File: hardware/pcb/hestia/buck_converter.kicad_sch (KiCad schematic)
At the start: 20 parts, among them U1 LM2655MTC-3.3/NOPB

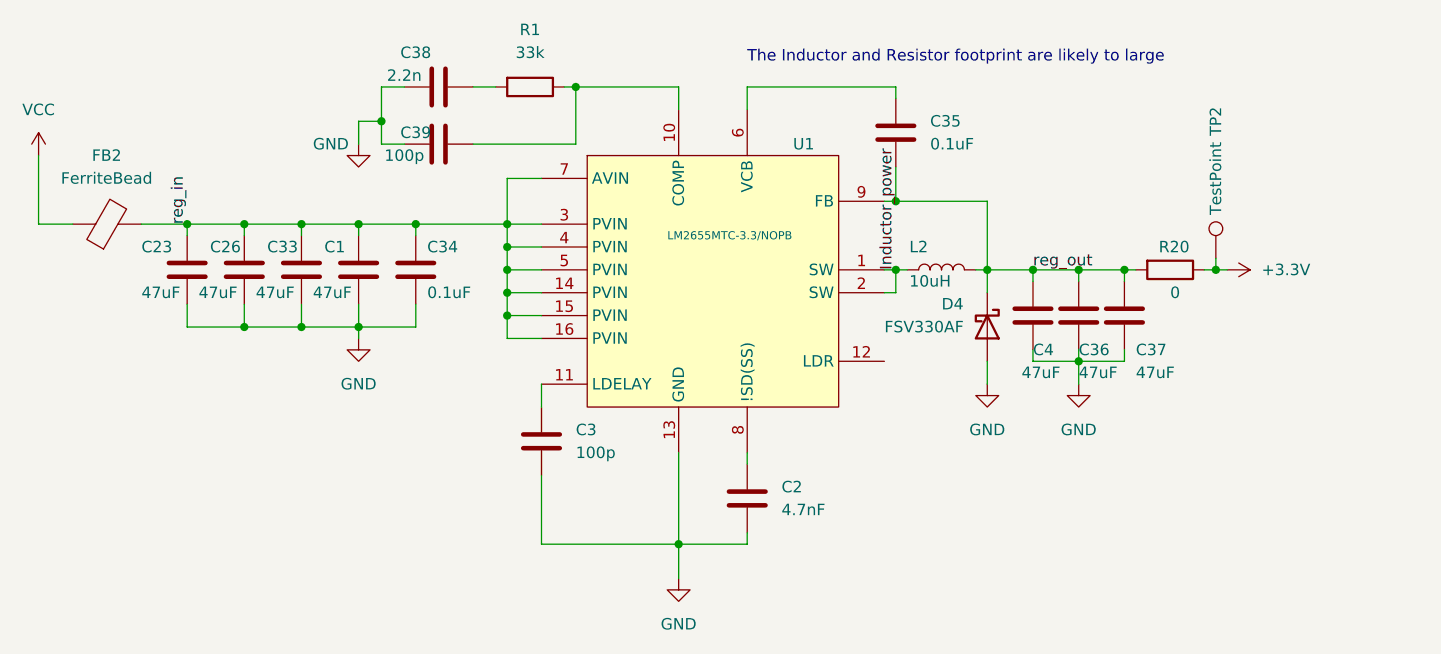
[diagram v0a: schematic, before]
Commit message: edit some component values
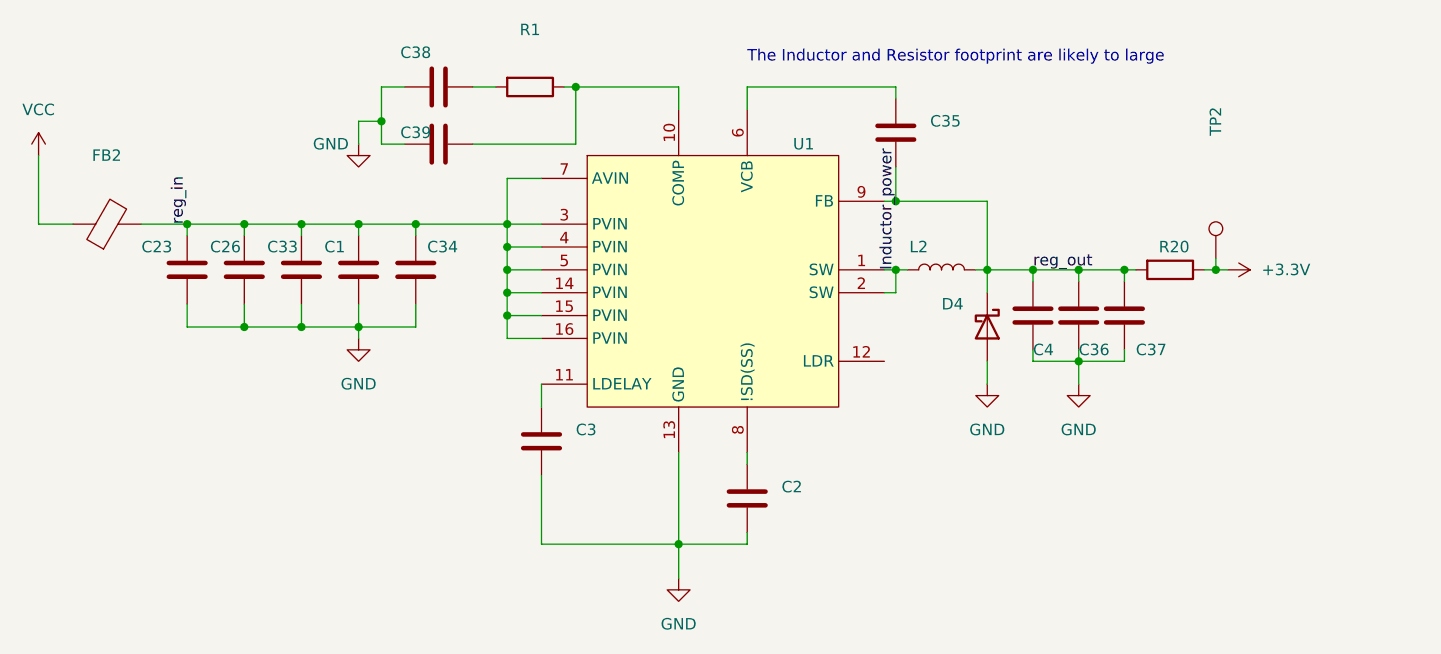
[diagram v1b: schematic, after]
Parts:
- C1, C23, C26, C33, C36, C37, C4: value 47uF -> (none); footprint Capacitor_SMD:C_0805_2012Metric_Pad1.18x1.45mm_HandSolder -> (none)
- C2: value 4.7nF -> (none); footprint Capacitor_SMD:C_0603_1608Metric_Pad1.08x0.95mm_HandSolder -> (none)
- C3, C39: value 100p -> (none); footprint Capacitor_SMD:C_0603_1608Metric_Pad1.08x0.95mm_HandSolder -> (none)
- C34, C35: value 0.1uF -> (none); footprint Capacitor_SMD:C_0603_1608Metric_Pad1.08x0.95mm_HandSolder -> (none)
- C38: value 2.2n -> (none); footprint Capacitor_SMD:C_0603_1608Metric_Pad1.08x0.95mm_HandSolder -> (none)
- D4: value FSV330AF -> (none); footprint Hestia:DO-214AD (SMAF) -> (none)
- FB2: value FerriteBead -> (none); footprint Resistor_SMD:R_0805_2012Metric_Pad1.20x1.40mm_HandSolder -> (none)
- L2: value 10uH -> (none); footprint Inductor_SMD:L_Coilcraft_LPS5030 -> (none)
- R1: value 33k -> (none); footprint Resistor_SMD:R_0603_1608Metric_Pad0.98x0.95mm_HandSolder -> (none)
- R20: value 0 -> (none); footprint Resistor_SMD:R_1210_3225Metric_Pad1.30x2.65mm_HandSolder -> (none)
- TP2: value TestPoint -> (none); footprint TestPoint:TestPoint_Pad_2.0x2.0mm -> (none)
- U1: value LM2655MTC-3.3/NOPB -> (none); footprint Package_SO:TSSOP-16_4.4x5mm_P0.65mm -> (none)

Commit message: Terminate pin 12 (LDR) on LM2655 to fix ERC warning
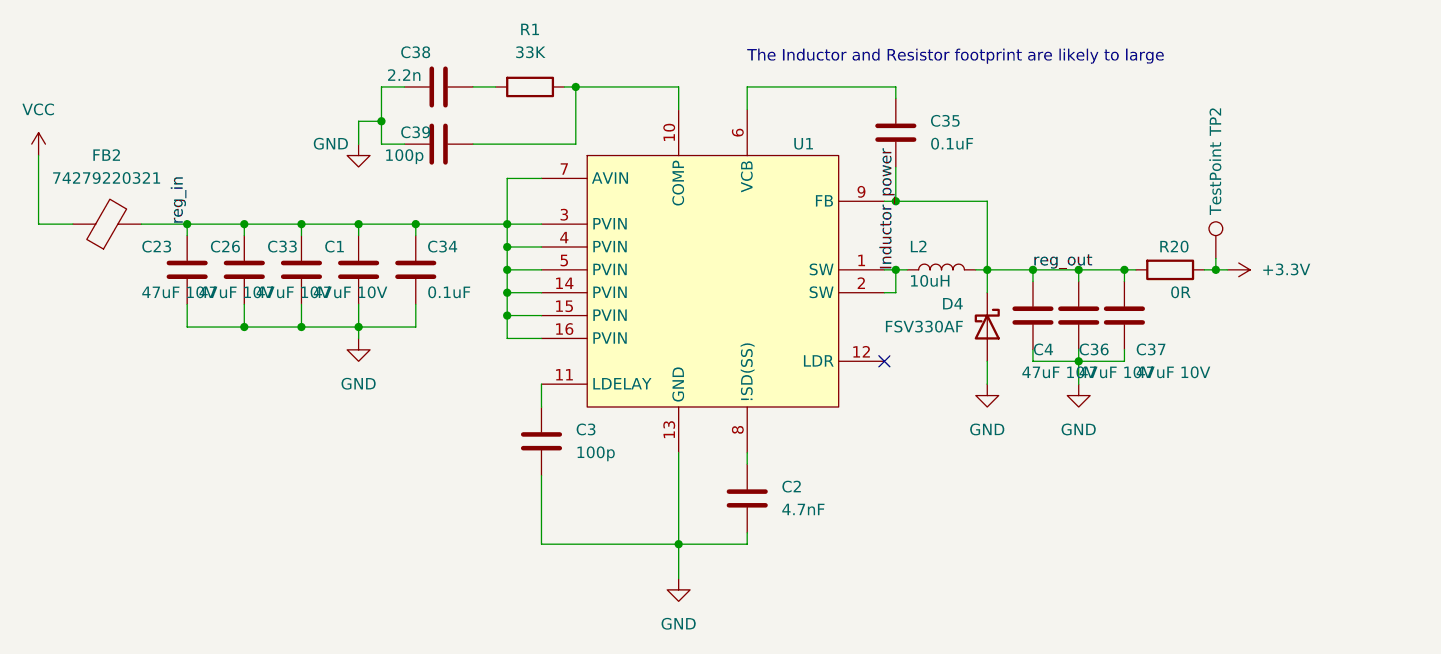
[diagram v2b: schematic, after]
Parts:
- C1, C23, C26, C33, C36, C37, C4: value (none) -> 47uF 10V; footprint (none) -> Capacitor_SMD:C_0805_2012Metric_Pad1.18x1.45mm_HandSolder
- C2: value (none) -> 4.7nF; footprint (none) -> Capacitor_SMD:C_0603_1608Metric_Pad1.08x0.95mm_HandSolder
- C3, C39: value (none) -> 100p; footprint (none) -> Capacitor_SMD:C_0603_1608Metric_Pad1.08x0.95mm_HandSolder
- C34, C35: value (none) -> 0.1uF; footprint (none) -> Capacitor_SMD:C_0603_1608Metric_Pad1.08x0.95mm_HandSolder
- C38: value (none) -> 2.2n; footprint (none) -> Capacitor_SMD:C_0603_1608Metric_Pad1.08x0.95mm_HandSolder
- D4: value (none) -> FSV330AF; footprint (none) -> Hestia:DO-214AD (SMAF)
- FB2: value (none) -> 74279220321; footprint (none) -> Resistor_SMD:R_0805_2012Metric_Pad1.20x1.40mm_HandSolder
- L2: value (none) -> 10uH; footprint (none) -> Inductor_SMD:L_Coilcraft_LPS5030
- R1: value (none) -> 33K; footprint (none) -> Resistor_SMD:R_0603_1608Metric_Pad0.98x0.95mm_HandSolder
- R20: value (none) -> 0R; footprint (none) -> Resistor_SMD:R_1210_3225Metric_Pad1.30x2.65mm_HandSolder
- TP2: value (none) -> TestPoint; footprint (none) -> TestPoint:TestPoint_Pad_2.0x2.0mm
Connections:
- no-connect marks 0 -> 1

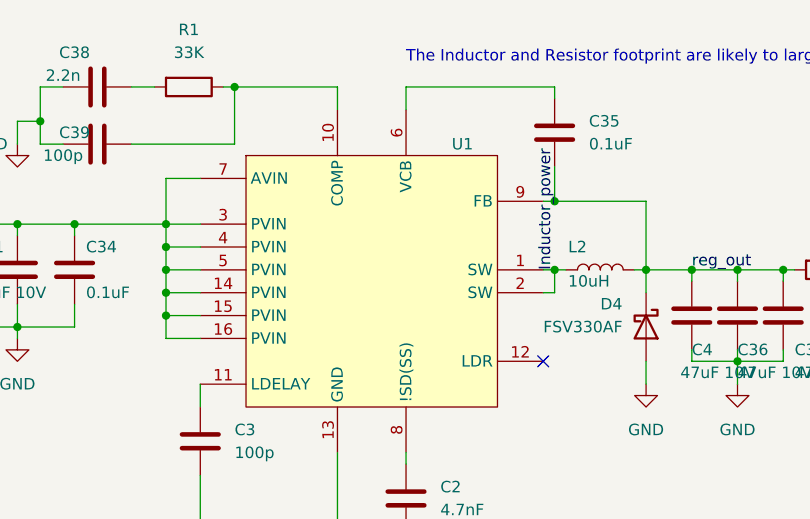
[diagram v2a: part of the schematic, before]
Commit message: Bump version to 2.0, add title to all schematic pages
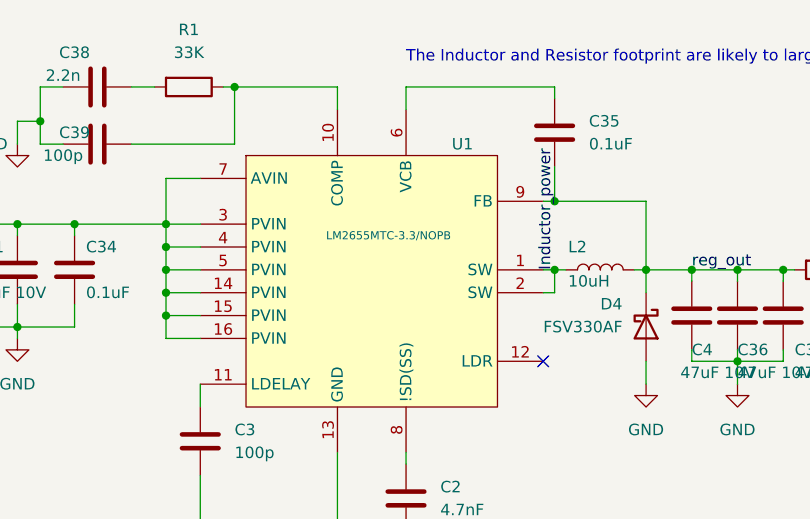
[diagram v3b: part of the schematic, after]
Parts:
- U1: value (none) -> LM2655MTC-3.3/NOPB; footprint (none) -> Package_SO:TSSOP-16_4.4x5mm_P0.65mm
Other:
- company: (none) -> Mawson Rovers
- title: (none) -> Hestia
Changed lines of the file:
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@@
 (kicad_sch (version 20211123) (generator eeschema)
   (paper "A4")
+  (title_block
+    (title "Hestia")
+    (date "2022-07-14")
+    (rev "2.0")
+    (company "Mawson Rovers")
+  )
   (junction (at 93.345 85.725) (diameter 0) (color 0 0 0 0)
   )
@@
       (effects (font (size 1.27 1.27)) (justify left))
     )
-    (property "Value" "" (id 1) (at 146.685 86.995 0)
+    (property "Value" "LM2655MTC-3.3/NOPB" (id 1) (at 146.685 86.995 0)
       (effects (font (size 0.9 0.9)) (justify left))
     )
-    (property "Footprint" "" (id 2) (at 155.575 95.885 0)
-      (effects (font (size 1.27 1.27)) hide)
-    )
+    (property "Footprint" "Package_SO:TSSOP-16_4.4x5mm_P0.65mm" (id 2) (at 155.575 95.885 0)
+      (effects (font (size 1.27 1.27)) hide)
+    )

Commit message: corrected diode placement
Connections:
- net Inductor_power: now also D4.1 (K)
- net reg_out: no longer D4.1 (K)
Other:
- moved on the sheet: D4
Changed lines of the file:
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@@
   (junction (at 192.405 90.805) (diameter 0) (color 0 0 0 0)
+  )
+  (junction (at 172.085 93.345) (diameter 0) (color 0 0 0 0)
   )
   (junction (at 114.935 74.295) (diameter 0) (color 0 0 0 0)
@@
     (stroke (width 0) (type default) (color 0 0 0 0))
   )
-  (wire (pts (xy 182.245 90.805) (xy 182.245 93.345))
-    (stroke (width 0) (type default) (color 0 0 0 0))
-  )
   (wire (pts (xy 99.695 97.155) (xy 106.045 97.155))
     (stroke (width 0) (type default) (color 0 0 0 0))
@@
     (stroke (width 0) (type default) (color 0 0 0 0))
   )
-  (wire (pts (xy 182.245 100.965) (xy 182.245 103.505))
+  (wire (pts (xy 172.085 100.965) (xy 172.085 103.505))
     (stroke (width 0) (type default) (color 0 0 0 0))
   )
@@
     (pin "2")
   )
-  (symbol (lib_id "Device:D_Schottky") (at 182.245 97.155 270) (unit 1)
-    (in_bom yes) (on_board yes)
-    (property "Reference" "D4" (id 0) (at 177.165 94.615 90)
-      (effects (font (size 1.27 1.27)) (justify left))
-    )
-    (property "Value" "FSV330AF" (id 1) (at 170.815 97.155 90)
-      (effects (font (size 1.27 1.27)) (justify left))
-    )
-    (property "Footprint" "Hestia:DO-214AD (SMAF)" (id 2) (at 182.245 97.155 0)
-      (effects (font (size 1.27 1.27)) hide)
-    )
-    (property "Datasheet" "~" (id 3) (at 182.245 97.155 0)
+  (symbol (lib_id "Device:D_Schottky") (at 172.085 97.155 270) (unit 1)
+    (in_bom yes) (on_board yes)
+    (property "Reference" "D4" (id 0) (at 167.005 94.615 90)
+      (effects (font (size 1.27 1.27)) (justify left))
+    )
+    (property "Value" "FSV330AF" (id 1) (at 160.655 97.155 90)
+      (effects (font (size 1.27 1.27)) (justify left))
+    )
+    (property "Footprint" "Hestia:DO-214AD (SMAF)" (id 2) (at 172.085 97.155 0)
+      (effects (font (size 1.27 1.27)) hide)
+    )
+    (property "Datasheet" "~" (id 3) (at 172.085 97.155 0)
       (effects (font (size 1.27 1.27)) hide)
     )
@@
     (pin "2")
   )
-  (symbol (lib_id "power:GND") (at 182.245 103.505 0) (unit 1)
+  (symbol (lib_id "power:GND") (at 172.085 103.505 0) (unit 1)
     (in_bom yes) (on_board yes) (fields_autoplaced)
-    (property "Reference" "#PWR04" (id 0) (at 182.245 109.855 0)
-      (effects (font (size 1.27 1.27)) hide)
-    )
-    (property "Value" "GND" (id 1) (at 182.245 108.585 0))
-    (property "Footprint" "" (id 2) (at 182.245 103.505 0)
-      (effects (font (size 1.27 1.27)) hide)
-    )
-    (property "Datasheet" "" (id 3) (at 182.245 103.505 0)
-      (effects (font (size 1.27 1.27)) hide)
-    )
+    (property "Reference" "#PWR04" (id 0) (at 172.085 109.855 0)
+      (effects (font (size 1.27 1.27)) hide)
+    )
+    (property "Value" "GND" (id 1) (at 172.085 108.585 0))
+    (property "Footprint" "" (id 2) (at 172.085 103.505 0)
+      (effects (font (size 1.27 1.27)) hide)
+    )
+    (property "Datasheet" "" (id 3) (at 172.085 103.505 0)
+      (effects (font (size 1.27 1.27)) hide)
+    )

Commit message: correct C35 capcitor placement
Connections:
- net Inductor_power: now also C35.2
- net reg_out: no longer C35.2
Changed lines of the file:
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@@
   (junction (at 106.045 85.725) (diameter 0) (color 0 0 0 0)
-  )
-  (junction (at 172.085 83.185) (diameter 0) (color 0 0 0 0)
   )
   (junction (at 128.905 93.345) (diameter 0) (color 0 0 0 0)
@@
     (stroke (width 0) (type default) (color 0 0 0 0))
   )
+  (wire (pts (xy 172.085 79.375) (xy 172.085 90.805))
+    (stroke (width 0) (type default) (color 0 0 0 0))
+  )
   (wire (pts (xy 76.835 85.725) (xy 80.645 85.725))
     (stroke (width 0) (type default) (color 0 0 0 0))
@@
     (stroke (width 0) (type default) (color 0 0 0 0))
   )
-  (wire (pts (xy 172.085 83.185) (xy 182.245 83.185))
+  (wire (pts (xy 170.815 83.185) (xy 182.245 83.185))
     (stroke (width 0) (type default) (color 0 0 0 0))
   )
@@
     (stroke (width 0) (type default) (color 0 0 0 0))
   )
-  (wire (pts (xy 170.815 83.185) (xy 172.085 83.185))
-    (stroke (width 0) (type default) (color 0 0 0 0))
-  )
   (wire (pts (xy 114.935 76.835) (xy 114.935 74.295))
     (stroke (width 0) (type default) (color 0 0 0 0))
   )
-  (wire (pts (xy 172.085 79.375) (xy 172.085 83.185))
-    (stroke (width 0) (type default) (color 0 0 0 0))
-  )

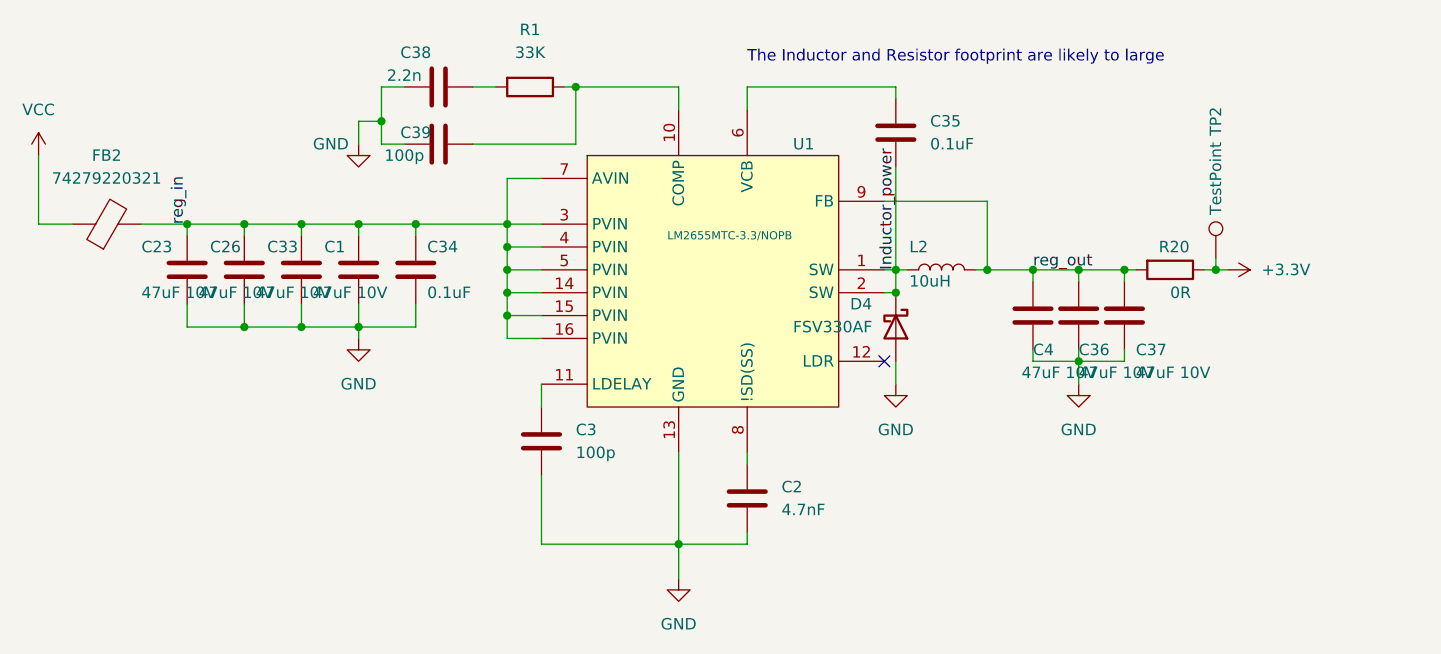
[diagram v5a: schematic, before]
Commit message: don't update pcb from schematic yet. added and changed footprint info on schematic for 1.5mm pitch term pads, crystals, jtag vcc jumper. a bunch of components are out of sync with the pcb, the schematic is unaware that the components are already on the PCB. some components from the first versions were not in the hestia parts library - hopefully this commit adds them back? was a commit made without a pull?
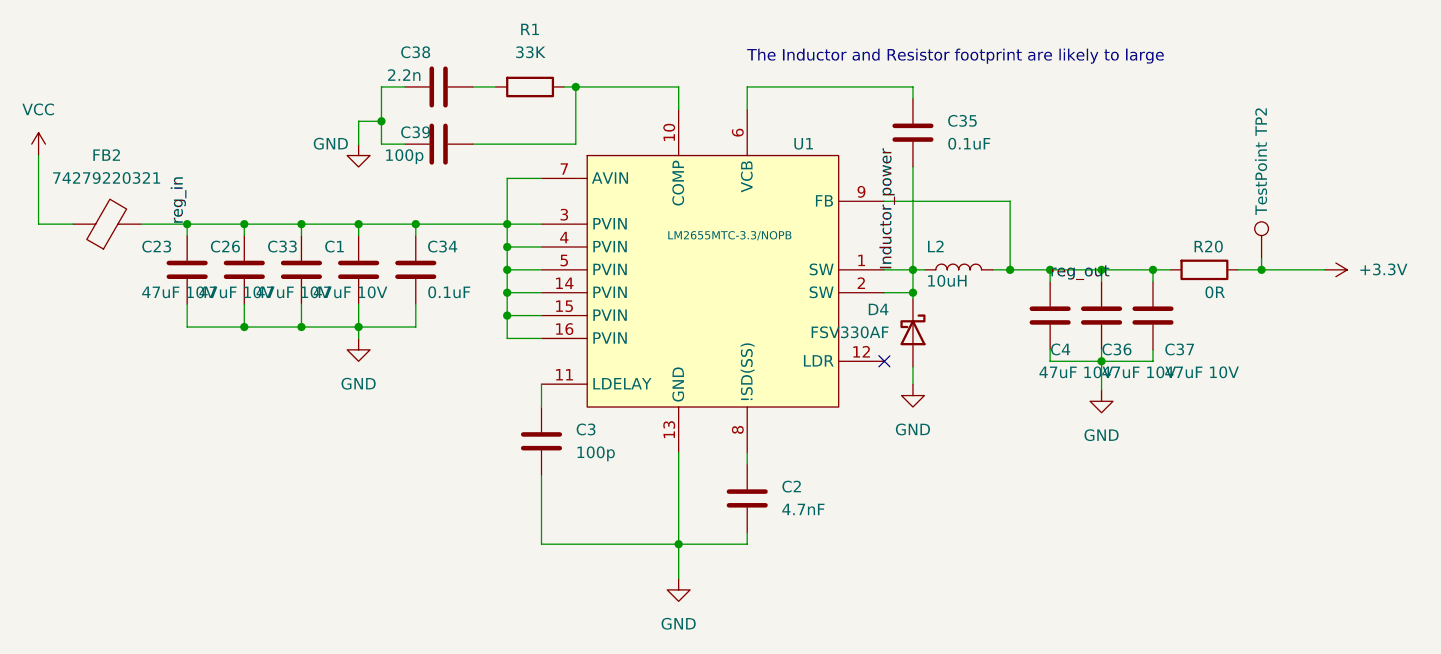
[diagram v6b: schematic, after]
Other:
- moved on the sheet: C35, C36, C37, C4, D4, L2, R20, TP2

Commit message: add another indicator led. add heater indicator led. add chipbeads to u3 adc input circuits. widen 3.3V trace to accomodate routing for adc and i2c sensors that were on 5V VCC previosuly. untangled most of the i2c signals. move some led traces from uC.
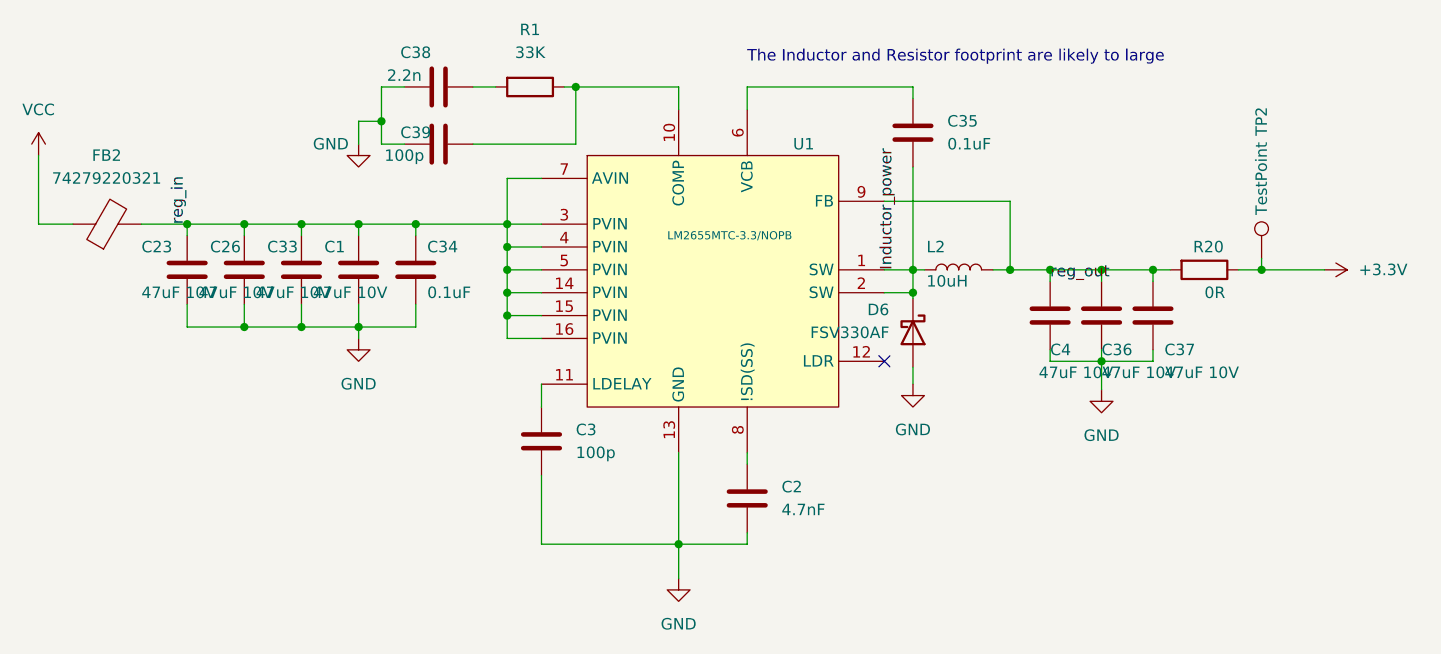
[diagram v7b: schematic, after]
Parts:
- renumbered D4 to D6
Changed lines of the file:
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@@
   (symbol (lib_id "Device:D_Schottky") (at 173.99 97.79 270) (unit 1)
     (in_bom yes) (on_board yes)
-    (property "Reference" "D4" (id 0) (at 168.91 95.25 90)
+    (property "Reference" "D6" (id 0) (at 168.91 95.25 90)
       (effects (font (size 1.27 1.27)) (justify left))
     )

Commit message: corrected typo
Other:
- note added: "The Inductor and Resistor footprint are likely too large"
- note removed: "The Inductor and Resistor footprint are likely to large"
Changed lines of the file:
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@@
     (stroke (width 0) (type default) (color 0 0 0 0))
   )
-  (text "The Inductor and Resistor footprint are likely to large"
+  (text "The Inductor and Resistor footprint are likely too large"
     (at 155.575 67.945 0)
     (effects (font (size 1.27 1.27)) (justify left bottom))
